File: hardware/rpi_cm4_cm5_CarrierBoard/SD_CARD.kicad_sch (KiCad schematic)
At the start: 17 parts, among them J1 DM3AT-SF-PEJM5, Q4 2N7002, Q5 2N7002, Q6 2N7002, U4 AP22913W6-7

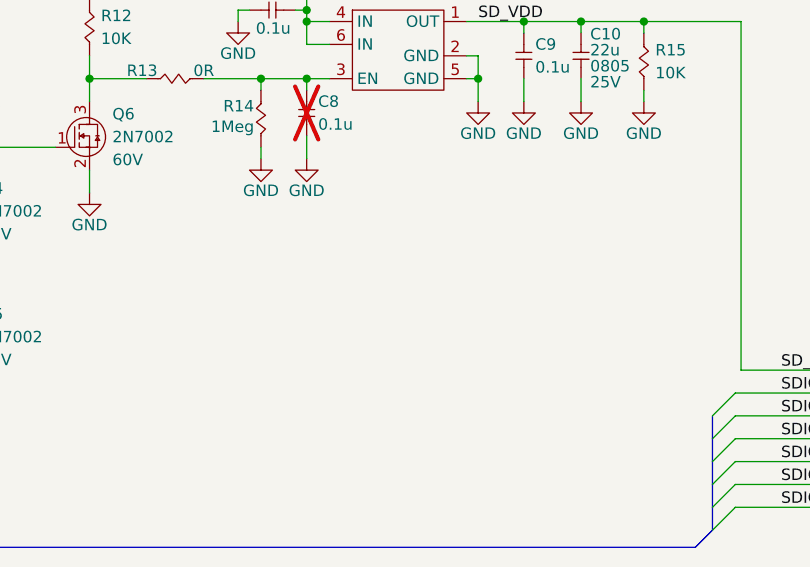
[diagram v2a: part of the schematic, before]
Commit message: Update schematic sheets (assembly variants, default cap / res notes)
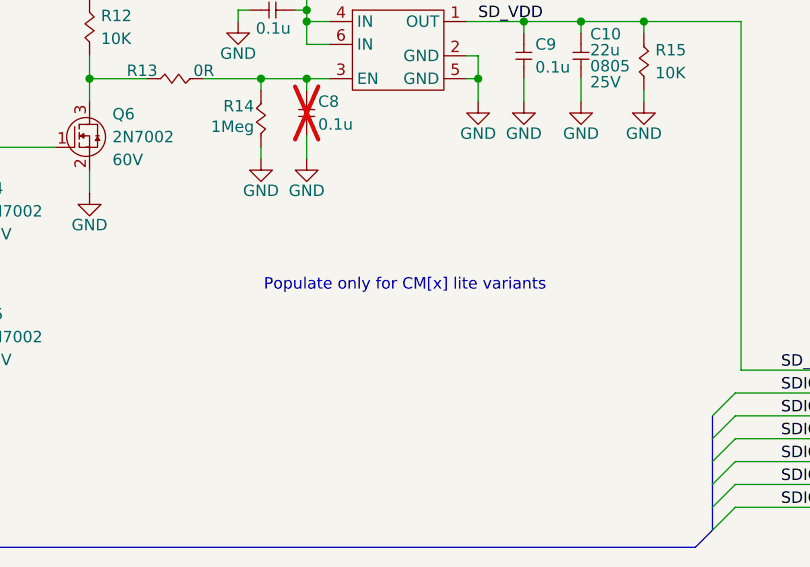
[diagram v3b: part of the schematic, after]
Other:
- note added: "Populate only for CM[x] lite variants"
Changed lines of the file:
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@@
 	(title_block
 		(title "RPI CMx Carrier")
-		(date "2026-02-20")
+		(date "2026-02-22")
 		(rev "2.00-0A")
 		(comment 1 "Jean-Francois Bilodeau")
@@
 		(members "SDIO_D0" "SDIO_D1" "SDIO_D2" "SDIO_D3" "SDIO_CLK" "SDIO_CMD")
 	)
+	(text "Populate only for CM[x] lite variants"
+		(exclude_from_sim no)
+		(at 137.922 83.312 0)
+		(effects
+			(font
+				(size 1.27 1.27)
+				(color 255 153 0 1)
+			)
+		)
+	)
 	(text "Resistors are 1% 1/16W 0402 unless otherwise noted\nCapacitors are 10% 50V X7R 0402 unless otherwise noted"
